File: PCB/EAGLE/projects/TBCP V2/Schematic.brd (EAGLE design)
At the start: 160 x 100 mm, 98 parts, among them J1 12 Supply, J2 TB Header, J3 FP Header, Q1 TRANSISTOR-FET_DMP2004K, U1 ESP32-DEVKITC, U2 TLE9201SG, U3 LM7805_SOT223

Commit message: TBCP 2.0 Board layout half done
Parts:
- removed E13: DPADS_PAD-0400-S, 52101-101-REV-A_v16:DPADS_0400-S
- removed R16: 100K, rcl:R2012
- removed S5: (no value), SparkFun-Switches:TACTILE_SWITCH_PTH_6.0MM
- removed SJ1: (no value), SparkFun-Jumpers:SMT-JUMPER_3_1-NC_PASTE_SILK
- removed SW2: (no value), One_Dimensional_Pong:SWITCH_SPST_SMD_A
- removed TP32, TP37, TP38, TP39, TP41: TESTPOINT_TPS-SMD-10SN, 52101-101-REV-A_v16:TESTPOINT_SMD-10SN
- added E2: DPADS_PAD-0400-S, 52101-101-REV-A_v16:DPADS_0400-S
- added J4: TB Header, Terminal 5.08 Pitch 6S 1757284:1757284
- added R18: (no value), rcl:R2012
- added S1: (no value), SparkFun-Retired:TACTILE-SWITCH-SMD
- added SW1: (no value), One_Dimensional_Pong:SWITCH_SPST_SMD_A
- added TP58, TP59, TP60, TP61, TP62, TP63, TP68, TP69, TP70, TP71, TP72, TP73, TP74, TP75: TESTPOINT_TPS-SMD-10SN, 52101-101-REV-A_v16:TESTPOINT_SMD-10SN
- added TP76: GPIO34, 52101-101-REV-A_v16:TESTPOINT_SMD-10SN
- added Z1: MM5Z10VT1G, MM5Z10VT1G:SODFL1608X70N
- C1, C2: value 0.1uf -> C0805C224J1RACTU; device 1C10X7R104K050B:CAPRR254W51L508T318H635P -> C0805C224J1RACTU:C0805
- D6: value 1N4740A-TR -> 150080AS75000; device Diodes-2:DO-41 -> Wurth_LEDs_WL-SMCW:WL-SMCW_0805
- J1: value 12 Supply -> ADS1115; device Terminal 5.08 Pitch 2S :1757284 -> ADS1115:ADS111X
- J2: value TB Header -> FP Header
- J3: value FP Header -> 12 Supply; device Terminal 5.08 Pitch 6S 1757284:1757284 -> Terminal 5.08 Pitch 2S :1757284
- Q1: value TRANSISTOR-FET_DMP2004K -> DMP4025LK3Q-13; device 52101-101-REV-A_v16:TRANSISTOR-FET_SOT23 -> DMP4025LK3Q-13:DMP4025LK3Q13
- R1, R3, R5: value 5k -> (none); device rcl:0207/10 -> rcl:R2012
- R10, R12, R14: value (none) -> 8000
- R11, R13, R9: value (none) -> 100k
- R15: value (none) -> 100K
- R17: value 91A1A-B28-B15L -> (none); device Potentiometer_Trimmers:91A1A-B28-B15L-ND -> rcl:R2012
- R2, R4, R6: value 3.3k -> (none); device rcl:0207/10 -> rcl:R2012
- S2, S3, S4: device SparkFun-Switches:TACTILE_SWITCH_PTH_6.0MM -> SparkFun-Retired:TACTILE-SWITCH-SMD
- TP13: value 3V3 -> TESTPOINT_TPS-SMD-10SN
- TP14: value EN -> TESTPOINT_TPS-SMD-10SN
- TP15: value GPIO36 -> TESTPOINT_TPS-SMD-10SN
- TP16: value GPIO39 -> TESTPOINT_TPS-SMD-10SN
- TP17: value GPIO34 -> TESTPOINT_TPS-SMD-10SN
- TP18: value GPIO35 -> TESTPOINT_TPS-SMD-10SN
- TP19: value GPIO32 -> TESTPOINT_TPS-SMD-10SN
- TP33: value TESTPOINT_TPS-SMD-10SN -> 3V3
- TP34: value TESTPOINT_TPS-SMD-10SN -> EN
- TP35: value TESTPOINT_TPS-SMD-10SN -> GPIO36
- TP36: value TESTPOINT_TPS-SMD-10SN -> GPIO39
- TP40: value TESTPOINT_TPS-SMD-10SN -> GPIO35
- TP42: value TESTPOINT_TPS-SMD-10SN -> GPIO32
- U1: value ESP32-DEVKITC -> 7805; device ESP32-DEVKITC:MODULE_ESP32-DEVKITC -> IC_Power-Management:SOT230P700X170-4
- U2: value TLE9201SG -> ESP32-DEVKITC; device TLE9201SG:IC_TLE9201SG -> ESP32-DEVKITC:MODULE_ESP32-DEVKITC
- U3: value LM7805_SOT223 -> TLE9201SG; device IC_Power-Management:SOT230P700X170-4 -> TLE9201SG:IC_TLE9201SG
- moved TP29 252.1 mm to (138.4, 17.8), turned to 90 degrees
- moved TP54 225.6 mm to (128.3, 17.8), turned to 90 degrees
- moved R15 214.7 mm to (111.8, 8.89), turned to 270 degrees
- moved R11 211.5 mm to (111.8, 27.9), turned to 270 degrees
- moved TP5 209.6 mm to (106.7, 55.9), flipped to the bottom, turned to 90 degrees
- moved TP4 202.4 mm to (104.1, 55.9), flipped to the bottom, turned to 90 degrees
- moved J2 197.2 mm to (152.4, 47.0), turned to 180 degrees
- moved Q1 195.4 mm to (99.1, 8.89), turned to 90 degrees
- moved TP3 195.2 mm to (101.6, 55.9), flipped to the bottom, turned to 90 degrees
- moved TP10 189.6 mm to (119.4, 55.9), flipped to the bottom, turned to 90 degrees
- moved C2 189.1 mm to (96.5, 31.8), turned to 270 degrees
- moved R13 188.4 mm to (106.7, 33.0), turned to 270 degrees
- moved TP2 188.0 mm to (99.1, 55.9), flipped to the bottom, turned to 90 degrees
- moved C1 186.8 mm to (96.5, 19.1), turned to 90 degrees
- moved R14 186.0 mm to (101.6, 43.2), turned to 270 degrees
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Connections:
- removed net FB_TB_INV: TP19.TP, U1.7
- removed net FP_FB_SCALED: R1.1, R2.2, TP17.TP, TP53.TP, U1.5
- removed net LED_SIG1: S3.3
- removed net LED_SIG2: S4.3
- removed net LED_SIG3: S5.3
- removed net N$6: TP37.TP, U1.33
- removed net TB_FB_INV_SCALED: R3.1, R4.2, TP52.TP
- removed net TB_FB_SCALED: R5.1, R6.2, SJ1.3, TP51.TP
- removed net TB_FB_SJ: SJ1.2
- removed net TB_SJ: TP18.TP, U1.6
- new net ADDR: J1.5, TP5.TP
- new net ADS1115_A0: J1.7, R14.2, R9.1, TP7.TP
- new net ADS1115_A1: J1.8, R12.2, R13.1, TP8.TP
- new net ADS1115_A2: J1.9, R10.2, R11.1, TP9.TP
- new net ADS1115_A4: J1.10, TP10.TP
- new net BNT_SIG1: R1.1, S2.1, S2.2
- new net BNT_SIG2: R3.1, S3.1, S3.2
- new net BNT_SIG3: R2.1, S1.1, S1.2
- new net BNT_SIG4: R5.1, S4.1, S4.2
- new net N$36: Q1.2, SW1.2
- new net N$37: TP42.TP, U2.7
- new net N$41: J1.6, TP6.TP
- new net SCL: J1.3, TP12.TP, TP3.TP, U2.36
- new net SDA: J1.4, TP15.TP, TP4.TP, U2.33
- net 0VDC: now also C1.1, C2.1, D6.1, J2.3, J2.5, J3.2, J4.6, R1.2, R10.1, R12.1, R14.1, R15.1, R2.2, R3.2, R5.2, TP16.TP, TP2.TP, TP30.TP, TP48.TP, TP68.TP, TP71.TP, TP75.TP, U1.2, U1.4, U2.14, U2.32, U2.38, U3.10, U3.13, U3.3, U3.6, U3.8, U3.9; no longer C1.2, C2.2, J2.6, J3.3, J3.5, R12.2, R13.2, R14.2, R15.2, R16.1, R17.3, R2.1, R4.1, R6.1, TP11.TP, TP26.TP, TP32.TP, TP38.TP, TP6.TP, TP9.TP, U1.14, U1.32, U1.38, U2.10, U2.13, U2.3, U2.6, U2.8, U2.9, U3.2, U3.4
- net 12VDC: now also C1.2, E2.PAD, TP59.TP, U1.1, U3.4, Z1.1; no longer C1.1, D6.C, E13.PAD, Q1.2, R7.2, SW2.1, U2.4, U3.1
- net 3.3VDC: now also J1.1, R7.2, S1.3, S1.4, S2.4, S3.3, S3.4, S4.3, S4.4, TP1.TP, TP33.TP, TP60.TP, U2.1, U3.2; no longer R17.1, TP13.TP, U1.1, U2.2
- net 5VDC: now also C2.2, J2.1, J2.6, J4.2, R18.2, TP53.TP, TP62.TP, TP63.TP, TP72.TP, U1.3, U2.19; no longer C2.1, J3.1, J3.2, J3.6, R8.2, TP1.TP, TP12.TP, TP7.TP, TP8.TP, U1.19, U3.3
- net FP_FB: now also J2.4, R11.2, TP73.TP; no longer J3.4, R1.2, TP10.TP
- net HBRDIGE_DISABLE: now also TP22.TP, TP56.TP, U2.26, U3.11; no longer TP44.TP, TP54.TP, U1.26, U2.11
- net HBRIDGE_DIRECTION: now also TP23.TP, TP61.TP, U2.25, U3.1; no longer TP45.TP, TP56.TP, U1.25, U2.1
- net HBRIDGE_PWM: now also TP24.TP, TP57.TP, U2.24, U3.12; no longer TP46.TP, TP55.TP, U1.24, U2.12
- net M0+: now also J4.3, TP29.TP, TP58.TP, U3.5; no longer J2.3, TP3.TP, U2.5
- net M0-: now also J4.5, TP55.TP, TP70.TP, U3.7; no longer J2.5, TP5.TP, U2.7
- net N$1: now also J3.1, SW1.3; no longer J1.1, SW2.2
- net N$10: now also TP20.TP, U2.28; no longer TP42.TP, U1.28
- net N$11: now also TP21.TP, U2.27; no longer TP43.TP, U1.27
- net N$12: now also D2.2, R4.1; no longer D4.2, R10.1
- net N$13: now also D1.2, R6.1; no longer D5.2, R11.1
- net N$14: now also R6.2, R8.2; no longer R11.2
- net N$15: now also TP25.TP, U2.23; no longer TP47.TP, U1.23
- net N$16: now also TP26.TP, U2.22; no longer TP48.TP, U1.22
- net N$17: now also TP27.TP, U2.21; no longer TP49.TP, U1.21
- net N$18: now also TP28.TP, U2.20; no longer TP50.TP, U1.20
- net N$19: now also TP34.TP, U2.2; no longer TP14.TP, U1.2
- net N$2: now also D5.2; no longer D1.2
- net N$20: now also TP35.TP, U2.3; no longer TP15.TP, U1.3
- net N$21: now also TP36.TP, U2.4; no longer TP16.TP, U1.4
- net N$22: now also TP74.TP, U2.8; no longer TP20.TP, U1.8
- net N$23: now also TP43.TP, U2.9; no longer TP21.TP, U1.9
- net N$24: now also TP44.TP, U2.10; no longer TP22.TP, U1.10
- net N$25: now also TP45.TP, U2.11; no longer TP23.TP, U1.11
- net N$26: now also TP46.TP, U2.12; no longer TP24.TP, U1.12
- net N$27: now also TP47.TP, U2.13; no longer TP25.TP, U1.13
- net N$28: now also TP49.TP, U2.15; no longer TP27.TP, U1.15
- net N$29: now also TP50.TP, U2.16; no longer TP28.TP, U1.16
- net N$3: now also D6.2, R8.1; no longer TP34.TP, U1.36
- net N$30: now also TP51.TP, U2.17; no longer TP29.TP, U1.17
- net N$31: now also TP52.TP, U2.18; no longer TP30.TP, U1.18
- net N$32: now also R4.2; no longer R10.2
- net N$33: now also R17.2; no longer R9.2
- net N$34: now also TP76.TP, U2.5; no longer R12.1, R13.1, R14.1, R15.1, S2.1, S3.1, S4.1, S5.1
- net N$35: now also TP40.TP, U2.6; no longer R17.2, SJ1.1, TP57.TP
- net N$4: now also TP13.TP, U2.35; no longer TP35.TP, U1.35
- net N$5: now also TP14.TP, U2.34; no longer TP36.TP, U1.34
- net N$7: now also R15.2, Z1.2; no longer D6.A, R16.2
- net N$8: now also D4.2, R18.1; no longer D2.2, R8.1
- net N$9: now also R17.1; no longer R9.1
- net SPI_CLOCK: now also TP18.TP, U2.30; no longer TP40.TP, U1.30
- net SPI_CS: now also TP19.TP, U2.29; no longer TP41.TP, U1.29
- net SPI_MISO: now also TP17.TP, U2.31; no longer TP39.TP, U1.31
- net SPI_MOSI: now also TP11.TP, U2.37; no longer TP33.TP, U1.37
- net TB_FB: now also J4.4, R13.2, TP69.TP; no longer J2.4, R5.2, TP4.TP
- net TB_FB_INV: now also J4.1, R9.2, TP54.TP; no longer J2.1, R3.2, TP2.TP
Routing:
- net 3.3VDC: track 0.00 -> 166.8 mm, vias 0 -> 1
- net 5VDC: track 0.00 -> 162.4 mm
- net M0-: track 0.00 -> 114.3 mm
- net M0+: track 0.00 -> 95.9 mm
- net 12VDC: track 0.00 -> 71.6 mm
- net TB_FB: track 0.00 -> 50.3 mm
- net TB_FB_INV: track 0.00 -> 47.5 mm
- net FP_FB: track 0.00 -> 40.3 mm
- net ADS1115_A2: track 0.00 -> 31.9 mm
- net ADS1115_A1: track 0.00 -> 28.1 mm
- net BNT_SIG4: track 0.00 -> 26.8 mm
- net ADS1115_A0: track 0.00 -> 26.0 mm
- net N$1: track 0.00 -> 24.8 mm
- net 0VDC: track 0.00 -> 24.1 mm
- net BNT_SIG3: track 0.00 -> 17.1 mm
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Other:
- board text added: "0VDC"
- board text added: "3.3VDC"
- board text added: "5VDC"
- board text added: "EN"
- board text added: "GPIO09"
- board text added: "GPIO10"
- board text added: "GPIO11"
- board text added: "GPIO25"
- board text added: "GPIO26"
- board text added: "GPIO27"
- board text added: "GPIO32"
- board text added: "GPIO33"
- board text added: "GPIO34"
- board text added: "GPIO35"
- board text added: "GPIO36"
- board text added: "GPIO39"

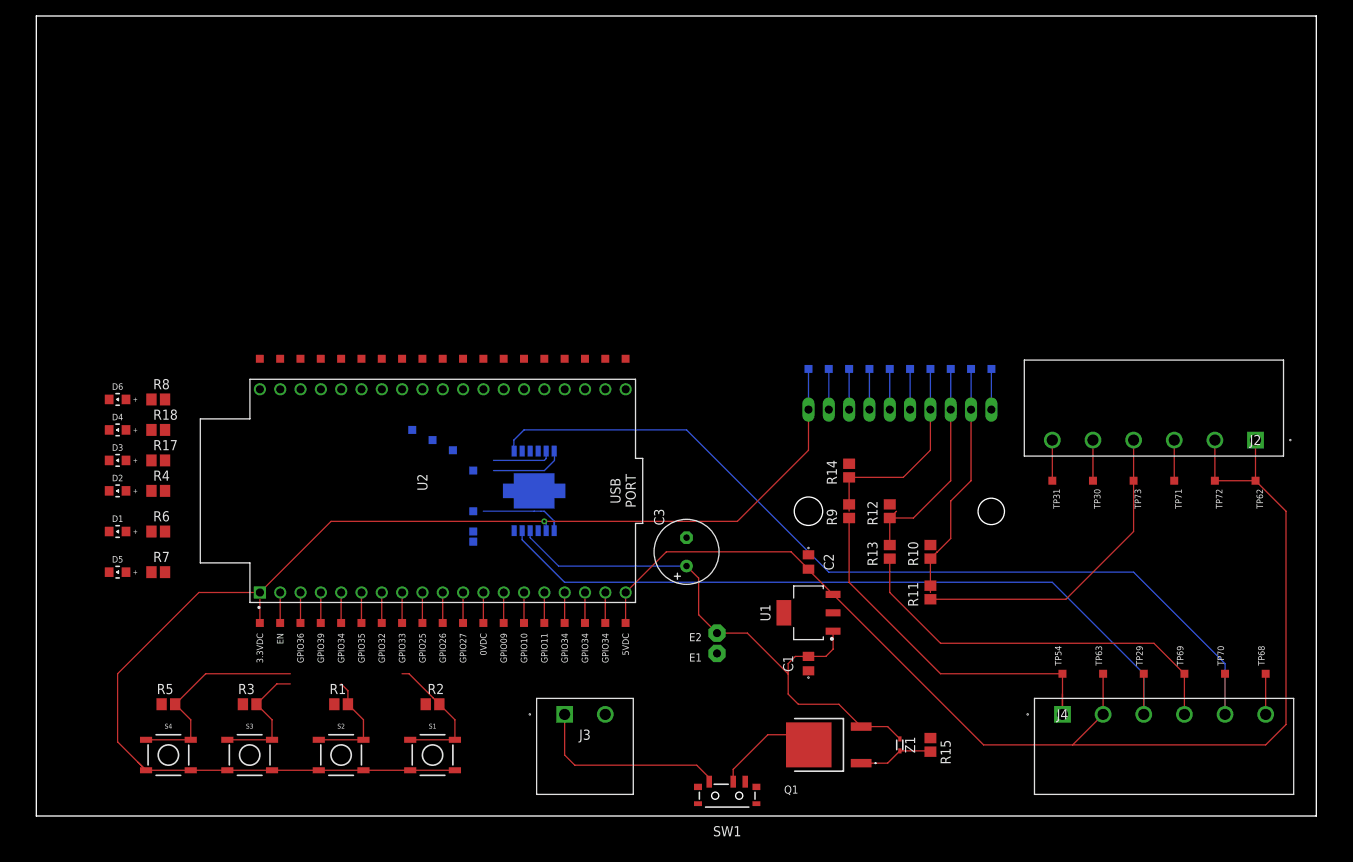
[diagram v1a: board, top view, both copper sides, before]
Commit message: Added Serial Studio for TB test
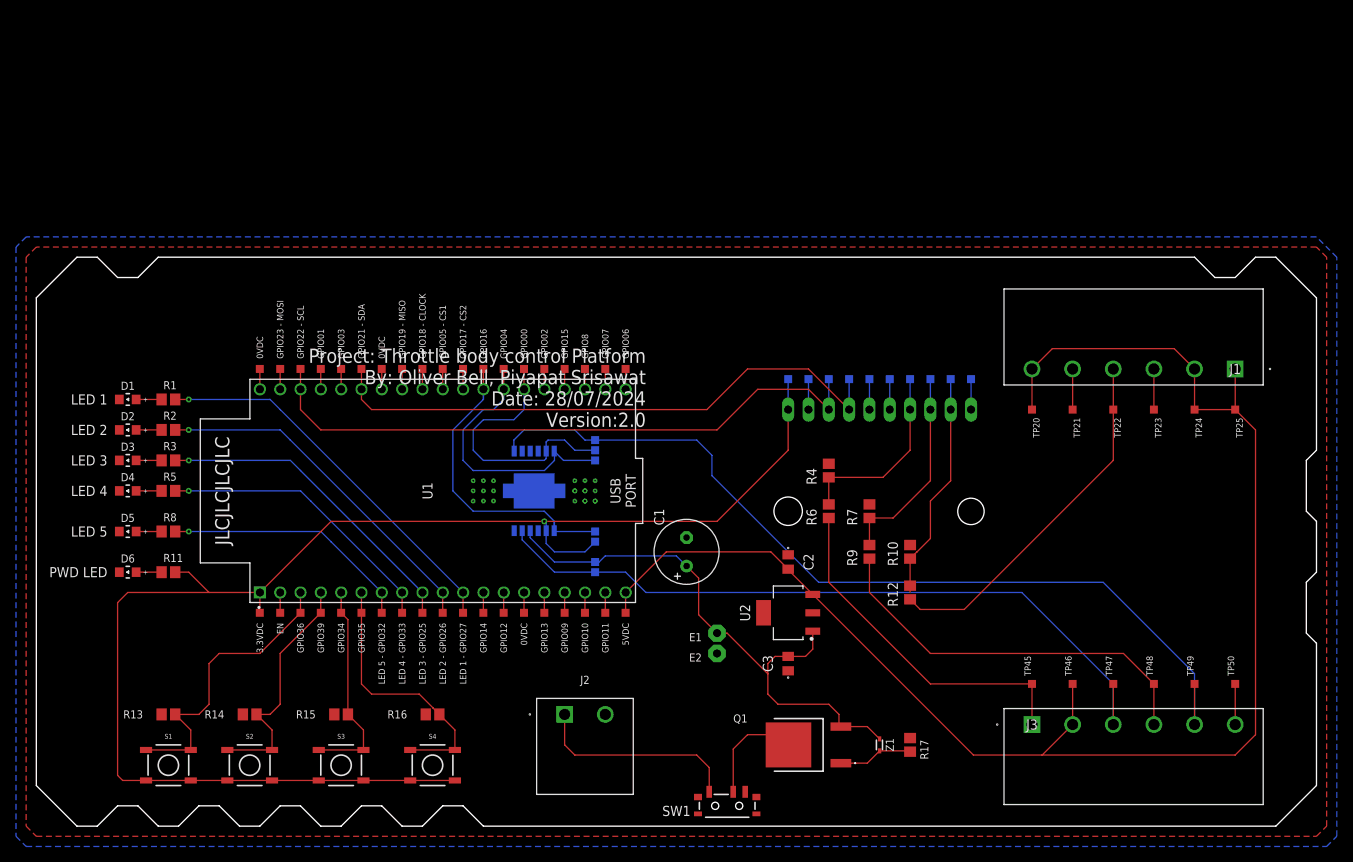
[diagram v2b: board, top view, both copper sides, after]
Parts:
- removed J4: TB Header, Terminal 5.08 Pitch 6S 1757284:1757284
- removed R18: (no value), rcl:R2012
- removed TP51, TP52, TP53, TP54, TP55, TP56, TP57, TP58, TP59, TP60, TP61, TP62, TP63, TP68, TP69, TP70, TP71, TP72, TP73, TP74, TP75: TESTPOINT_TPS-SMD-10SN, 52101-101-REV-A_v16:TESTPOINT_SMD-10SN
- removed TP76: GPIO34, 52101-101-REV-A_v16:TESTPOINT_SMD-10SN
- added J100: ADS1115, ADS1115:ADS111X
- added R16: (no value), rcl:R2012
- added TP100, TP101, TP102, TP103, TP104, TP105, TP106, TP107, TP108, TP109, TP110, TP111, TP112, TP113, TP114, TP115, TP116, TP37, TP38, TP39, TP41: TESTPOINT_TPS-SMD-10SN, 52101-101-REV-A_v16:TESTPOINT_SMD-10SN
- added TP32: GPIO32, 52101-101-REV-A_v16:TESTPOINT_SMD-10SN
- C1: value C0805C224J1RACTU -> (none); device C0805C224J1RACTU:C0805 -> BeagleBone_Blue_R3:E3,5-8
- C3: value (none) -> C0805C224J1RACTU; device BeagleBone_Blue_R3:E3,5-8 -> C0805C224J1RACTU:C0805
- J1: value ADS1115 -> FP Header; device ADS1115:ADS111X -> Terminal 5.08 Pitch 6S 1757284:1757284
- J2: value FP Header -> 12 Supply; device Terminal 5.08 Pitch 6S 1757284:1757284 -> Terminal 5.08 Pitch 2S :1757284
- J3: value 12 Supply -> TB Header; device Terminal 5.08 Pitch 2S :1757284 -> Terminal 5.08 Pitch 6S 1757284:1757284
- R11, R13: value 100k -> (none)
- R12: value 8000 -> 100k
- R14: value 8000 -> (none)
- R15: value 100K -> (none)
- R17: value (none) -> 100K
- R4, R7: value (none) -> 8000
- R6: value (none) -> 100k
- TP26: value TESTPOINT_TPS-SMD-10SN -> 3V3
- TP27: value TESTPOINT_TPS-SMD-10SN -> EN
- TP28: value TESTPOINT_TPS-SMD-10SN -> GPIO36
- TP29: value TESTPOINT_TPS-SMD-10SN -> GPIO39
- TP30: value TESTPOINT_TPS-SMD-10SN -> GPIO34
- TP31: value TESTPOINT_TPS-SMD-10SN -> GPIO35
- TP33: value 3V3 -> TESTPOINT_TPS-SMD-10SN
- TP34: value EN -> TESTPOINT_TPS-SMD-10SN
- TP35: value GPIO36 -> TESTPOINT_TPS-SMD-10SN
- TP36: value GPIO39 -> TESTPOINT_TPS-SMD-10SN
- TP40: value GPIO35 -> TESTPOINT_TPS-SMD-10SN
- TP42: value GPIO32 -> TESTPOINT_TPS-SMD-10SN
- U1: value 7805 -> ESP32-DEVKITC; device IC_Power-Management:SOT230P700X170-4 -> ESP32-DEVKITC:MODULE_ESP32-DEVKITC
- U2: value ESP32-DEVKITC -> 7805; device ESP32-DEVKITC:MODULE_ESP32-DEVKITC -> IC_Power-Management:SOT230P700X170-4
- moved TP29 103.2 mm to (35.6, 25.4), turned to 270 degrees
- moved R17 100.5 mm to (109.2, 8.89), turned to 270 degrees
- moved TP30 95.4 mm to (38.1, 25.4)
- moved R11 95.3 mm to (16.5, 30.5), turned to 0 degrees
- moved J2 92.9 mm to (66.0, 12.7), turned to 0 degrees
- moved R13 92.4 mm to (16.5, 12.7), turned to 180 degrees
- moved R7 89.2 mm to (104.1, 38.1), turned to 270 degrees
- moved TP31 87.9 mm to (40.6, 25.4)
- moved TP50 84.2 mm to (149.9, 16.5), turned to 90 degrees
- moved TP25 84.1 mm to (149.9, 50.8), turned to 270 degrees
- moved R4 83.9 mm to (99.1, 43.2), turned to 270 degrees
- moved R6 83.9 mm to (99.1, 38.1), turned to 270 degrees
- moved TP49 81.6 mm to (144.8, 16.5), turned to 90 degrees
- moved TP24 81.5 mm to (144.8, 50.8), turned to 270 degrees
- moved R14 80.9 mm to (26.7, 12.7), turned to 180 degrees
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- renumbered U3 to U100
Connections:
- removed net BNT_SIG1: R1.1, S2.1, S2.2
- removed net BNT_SIG2: R3.1, S3.1, S3.2
- removed net BNT_SIG3: R2.1, S1.1, S1.2
- removed net BNT_SIG4: R5.1, S4.1, S4.2
- removed net N$10: TP20.TP, U2.28
- removed net N$11: TP21.TP, U2.27
- removed net N$14: R6.2, R8.2
- removed net N$15: TP25.TP, U2.23
- removed net N$16: TP26.TP, U2.22
- removed net N$17: TP27.TP, U2.21
- removed net N$18: TP28.TP, U2.20
- removed net N$19: TP34.TP, U2.2
- removed net N$20: TP35.TP, U2.3
- removed net N$21: TP36.TP, U2.4
- removed net N$22: TP74.TP, U2.8
- removed net N$23: TP43.TP, U2.9
- removed net N$24: TP44.TP, U2.10
- removed net N$25: TP45.TP, U2.11
- removed net N$26: TP46.TP, U2.12
- removed net N$27: TP47.TP, U2.13
- removed net N$28: TP49.TP, U2.15
- removed net N$29: TP50.TP, U2.16
- removed net N$30: TP51.TP, U2.17
- removed net N$31: TP52.TP, U2.18
- removed net N$32: R4.2
- removed net N$33: R17.2
- removed net N$34: TP76.TP, U2.5
- removed net N$35: TP40.TP, U2.6
- removed net N$37: TP42.TP, U2.7
- removed net N$4: TP13.TP, U2.35
- removed net N$5: TP14.TP, U2.34
- removed net SPI_CS: TP19.TP, U2.29
- new net EN: TP27.TP, U1.2
- new net GPIO01: TP4.TP, U1.35
- new net GPIO02: TP15.TP, U1.24
- new net GPIO03: TP5.TP, U1.34
- new net GPIO06: TP19.TP, U1.20
- new net GPIO07: TP18.TP, U1.21
- new net GPIO08: TP17.TP, U1.22
- new net GPIO09: TP41.TP, U1.16
- new net GPIO10: TP42.TP, U1.17
- new net GPIO11: TP43.TP, U1.18
- new net GPIO12: TP38.TP, U1.13
- new net GPIO13: TP40.TP, U1.15
- new net GPIO14: TP37.TP, U1.12
- new net GPIO15: TP16.TP, U1.23
- new net GPIO25: R3.2, TP34.TP, U1.9
- new net GPIO26: R2.2, TP35.TP, U1.10
- new net GPIO27: R1.2, TP36.TP, U1.11
- new net GPIO32: R8.2, TP32.TP, U1.7
- new net GPIO33: R5.2, TP33.TP, U1.8
- new net GPIO34: R15.1, S3.1, S3.2, TP30.TP, U1.5
- new net GPIO35: R16.1, S4.1, S4.2, TP31.TP, U1.6
- new net GPIO36: R13.1, S1.1, S1.2, TP28.TP, U1.3
- new net GPIO39: R14.1, S2.1, S2.2, TP29.TP, U1.4
- new net SPI_CS1: TP10.TP, U1.29
- new net SPI_CS2: TP11.TP, U1.28
- net 0VDC: now also C1.-, C3.1, E2.PAD, J1.3, J1.5, J100.2, J2.2, J3.6, R13.2, R14.2, R15.2, R16.2, R17.1, R4.1, R7.1, TP1.TP, TP115.TP, TP21.TP, TP23.TP, TP39.TP, TP50.TP, TP7.TP, U1.14, U1.32, U1.38, U2.2, U2.4; no longer C1.1, C3.-, E1.PAD, J1.2, J2.3, J2.5, J3.2, J4.6, R1.2, R12.1, R14.1, R15.1, R2.2, R3.2, R5.2, TP16.TP, TP2.TP, TP30.TP, TP48.TP, TP68.TP, TP71.TP, TP75.TP, U1.2, U1.4, U2.14, U2.32, U2.38
- net 12VDC: now also C1.+, C3.2, E1.PAD, TP101.TP, U2.1; no longer C1.2, C3.+, E2.PAD, TP59.TP, U1.1
- net 3.3VDC: now also J100.1, R11.2, TP102.TP, TP116.TP, TP26.TP, U1.1; no longer J1.1, R7.2, TP1.TP, TP33.TP, TP60.TP, U2.1
- net 5VDC: now also J1.1, J1.2, J1.6, J3.2, TP20.TP, TP24.TP, TP25.TP, TP44.TP, TP46.TP, U1.19, U2.3; no longer J2.1, J2.2, J2.6, J4.2, R18.2, TP31.TP, TP53.TP, TP62.TP, TP63.TP, TP72.TP, U1.3, U2.19
- net ADDR: now also J100.5, TP112.TP; no longer J1.5, TP5.TP
- net ADS1115_A0: now also J100.7, R4.2, R6.1, TP110.TP; no longer J1.7, R14.2, R9.1, TP7.TP
- net ADS1115_A1: now also J100.8, R7.2, R9.1, TP109.TP; no longer J1.8, R12.2, R13.1, TP8.TP
- net ADS1115_A2: now also J100.9, R12.1, TP108.TP; no longer J1.9, R11.1, TP9.TP
- net ADS1115_A4: now also J100.10, TP107.TP; no longer J1.10, TP10.TP
- net FP_FB: now also J1.4, R12.2, TP22.TP; no longer J2.4, R11.2, TP73.TP
- net HBRDIGE_DISABLE: now also TP105.TP, TP14.TP, U1.25; no longer TP22.TP, TP56.TP, U2.26
- net HBRIDGE_DIRECTION: now also TP103.TP, TP12.TP, U1.27; no longer TP23.TP, TP61.TP, U2.25
- net HBRIDGE_PWM: now also TP104.TP, TP13.TP, U1.26; no longer TP24.TP, TP57.TP, U2.24
- net M0+: now also J3.3, TP100.TP, TP47.TP; no longer J4.3, TP29.TP, TP58.TP
- net M0-: now also J3.5, TP106.TP, TP49.TP; no longer J4.5, TP55.TP, TP70.TP
- net N$1: now also J2.1; no longer J3.1
- net N$12: now also D4.2, R5.1; no longer D2.2, R4.1
- net N$13: now also D5.2, R8.1; no longer D1.2, R6.1
- net N$2: now also D6.2, R11.1; no longer D5.2, R7.1
- net N$3: now also D1.2, R1.1; no longer D6.2, R8.1
- net N$41: now also J100.6, TP111.TP; no longer J1.6, TP6.TP
- net N$7: now also R17.2; no longer R15.2
- net N$8: now also D2.2, R2.1; no longer D4.2, R18.1
- net N$9: now also R3.1; no longer R17.1
- net SCL: now also J100.3, TP114.TP, U1.36; no longer J1.3, TP12.TP, U2.36
- net SDA: now also J100.4, TP113.TP, TP6.TP, U1.33; no longer J1.4, TP15.TP, TP4.TP, U2.33
- net SPI_CLOCK: now also TP9.TP, U1.30; no longer TP18.TP, U2.30
- net SPI_MISO: now also TP8.TP, U1.31; no longer TP17.TP, U2.31
- net SPI_MOSI: now also TP2.TP, U1.37; no longer TP11.TP, U2.37
- net TB_FB: now also J3.4, R9.2, TP48.TP; no longer J4.4, R13.2, TP69.TP
- net TB_FB_INV: now also J3.1, R6.2, TP45.TP; no longer J4.1, R9.2, TP54.TP
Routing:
- net SCL: track 5.08 -> 79.2 mm
- net SDA: track 5.08 -> 73.3 mm
- net GPIO27: track 0.00 -> 48.5 mm, vias 0 -> 1
- net GPIO26: track 0.00 -> 44.4 mm, vias 0 -> 1
- net GPIO25: track 0.00 -> 40.3 mm, vias 0 -> 1
- net GPIO36: track 0.00 -> 37.3 mm
- net GPIO33: track 0.00 -> 36.2 mm, vias 0 -> 1
- net GPIO35: track 0.00 -> 33.6 mm
- net GPIO32: track 0.00 -> 31.5 mm, vias 0 -> 1
- net GPIO39: track 0.00 -> 30.4 mm
- net HBRIDGE_DIRECTION: track 11.8 -> 39.9 mm
- net 5VDC: track 162.4 -> 189.9 mm
- net BNT_SIG4: track 26.8 -> 0.00 mm
- net GPIO34: track 0.00 -> 26.4 mm
- net HBRDIGE_DISABLE: track 7.61 -> 33.6 mm
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- added copper zone on layer 1, net 0VDC
- added copper zone on layer 16, net 0VDC1
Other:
- board size 160 x 100 mm -> 160 x 71.1 mm
- board text added: "GPIO00"
- board text added: "GPIO01"
- board text added: "GPIO02"
- board text added: "GPIO03"
- board text added: "GPIO04"
- board text added: "GPIO05 - CS1"
- board text added: "GPIO06"
- board text added: "GPIO07"
- board text added: "GPIO12"
- board text added: "GPIO13"
- board text added: "GPIO14"
- board text added: "GPIO15"
- board text added: "GPIO16"
- board text added: "GPIO17 - CS2"
- board text added: "GPIO18 - CLOCK"
- board text added: "GPIO19 - MISO"
- board text added: "GPIO21 - SDA"
- board text added: "GPIO22 - SCL"
- board text added: "GPIO23 - MOSI"
- board text added: "GPIO8"
- board text added: "JLCJLCJLCJLC"
- board text added: "LED 1"
- board text added: "LED 1 - GPIO27"
- board text added: "LED 2"
- board text added: "LED 2 - GPIO26"
- board text added: "LED 3"
- board text added: "LED 3 - GPIO25"
- board text added: "LED 4"
- board text added: "LED 4 - GPIO33"
- board text added: "LED 5"
- board text added: "LED 5 - GPIO32"
- board text added: "PWD LED"
- board text added: "Project: Throttle body control Platform By: Oliver Bell, Piyapat Srisawat Date: 28/07/2024 Version:2.0"
- board text removed: "GPIO25"
- board text removed: "GPIO26"
- board text removed: "GPIO27"
- board text removed: "GPIO32"
- board text removed: "GPIO33"
